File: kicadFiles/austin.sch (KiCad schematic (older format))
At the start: 474 parts, among them J1 TYPE-C-31-M12_13, J5 Conn_01x06_Male, Q1 AO4406AL, SW1 MXSwitch, SW10 MXSwitch, SW100 MXSwitch, SW101 MXSwitch, SW102 MXSwitch, SW103 MXSwitch, SW104 MXSwitch, SW105 MXSwitch, SW106 MXSwitch, SW107 MXSwitch, SW108 MXSwitch, SW109 MXSwitch, SW11 MXSwitch, SW110 MXSwitch, SW111 MXSwitch, SW112 MXSwitch, SW113 MXSwitch, SW114 MXSwitch, SW12 MXSwitch, SW13 MXSwitch, SW14 MXSwitch, SW15 MXSwitch, SW16 MXSwitch, SW17 MXSwitch, SW18 MXSwitch, SW19 MXSwitch, SW2 MXSwitch, SW20 MXSwitch, SW21 MXSwitch, SW22 MXSwitch, SW23 MXSwitch, SW24 MXSwitch, SW25 MXSwitch, SW26 MXSwitch, SW27 MXSwitch, SW28 MXSwitch, SW29 MXSwitch, SW3 MXSwitch, SW30 MXSwitch, SW31 MXSwitch, SW32 MXSwitch, SW33 MXSwitch, SW34 MXSwitch, SW35 MXSwitch, SW36 MXSwitch, SW37 MXSwitch, SW38 MXSwitch, SW39 MXSwitch, SW4 MXSwitch, SW40 MXSwitch, SW41 MXSwitch, SW42 MXSwitch, SW43 MXSwitch, SW44 MXSwitch, SW45 MXSwitch, SW46 MXSwitch, SW47 MXSwitch, SW48 MXSwitch, SW49 MXSwitch, SW5 MXSwitch, SW50 MXSwitch, SW51 MXSwitch, SW52 MXSwitch, SW53 MXSwitch, SW54 MXSwitch, SW55 MXSwitch, SW56 MXSwitch, SW57 MXSwitch, SW59 MXSwitch, SW6 MXSwitch, SW60 MXSwitch, SW61 MXSwitch, SW62 MXSwitch, SW63 MXSwitch, SW64 MXSwitch, SW65 MXSwitch, SW66 MXSwitch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

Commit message: Add LSHIFT ISO key, change LED_PWM pin
- The ISO 1.25U LShift was not added in the pre-Alpha version, even though the ISO Enter was supported. The ISO LShift and slash keys were added to the schematic.

- To accomodate for the change, every key of the fourth row from Z to the up arrow had to be moved a column right.

- The LED_PWM pin had to be reallocated from PB7 to PA6. Although the LEDs are provenly working with the last pin, it does not have hardware PWM, which is desirable. The new pin, PA6, is PWM capable. In order to accomodate this change, the Row3 pin had to be reallocated from PA6 to PB7.
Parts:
- added D34: 1N4148, acheronComponents:D_SOD-123, symbol Device:D
- added SW58: ANSI LShift, acheron_MX:MX225, symbol austin-rescue:MXSwitch-acheronSymbols
- added SW78: ISO Slash, acheron_MX:MX100, symbol austin-rescue:MXSwitch-acheronSymbols
- SW79: value MXSwitch -> ISO LShift; footprint acheron_MX:MX225 -> acheron_MX:MX125
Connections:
- net Col1: now also SW58.1 (Col)
- net Col10: now also SW87.1 (Col); no longer SW88.1 (Col)
- net Col11: now also SW88.1 (Col); no longer SW89.1 (Col)
- net Col12: now also SW89.1 (Col); no longer SW90.1 (Col)
- net Col13: now also SW90.1 (Col); no longer SW91.1 (Col)
- net Col14: now also SW91.1 (Col)
- net Col2: now also SW78.1 (Col); no longer SW80.1 (Col)
- net Col3: now also SW80.1 (Col); no longer SW81.1 (Col)
- net Col4: now also SW81.1 (Col); no longer SW82.1 (Col)
- net Col5: now also SW82.1 (Col); no longer SW83.1 (Col)
- net Col6: now also SW83.1 (Col); no longer SW84.1 (Col)
- net Col7: now also SW84.1 (Col); no longer SW85.1 (Col)
- net Col8: now also SW85.1 (Col); no longer SW86.1 (Col)
- net Col9: now also SW86.1 (Col); no longer SW87.1 (Col)
- net LED_PWM: now also U1.16 (SPI1_MISO/I2S1_MCK/TIM3_CH1/ADCIN6/PA6); no longer U1.43 (I2C1_SDA/PB7)
- net Row3: now also U1.43 (I2C1_SDA/PB7); no longer U1.16 (SPI1_MISO/I2S1_MCK/TIM3_CH1/ADCIN6/PA6)
- net Row5: now also D34.1 (K); no longer D89.1 (K), D91.1 (K)
- net at D79.2 (A), SW79.2 (Row): now also SW58.2 (Row)
- new net: D34.2 (A), SW78.2 (Row)
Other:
- moved on the sheet: D80, D81, D82, D83, D84, D85, D86, D87, D88, D89, D90, D91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

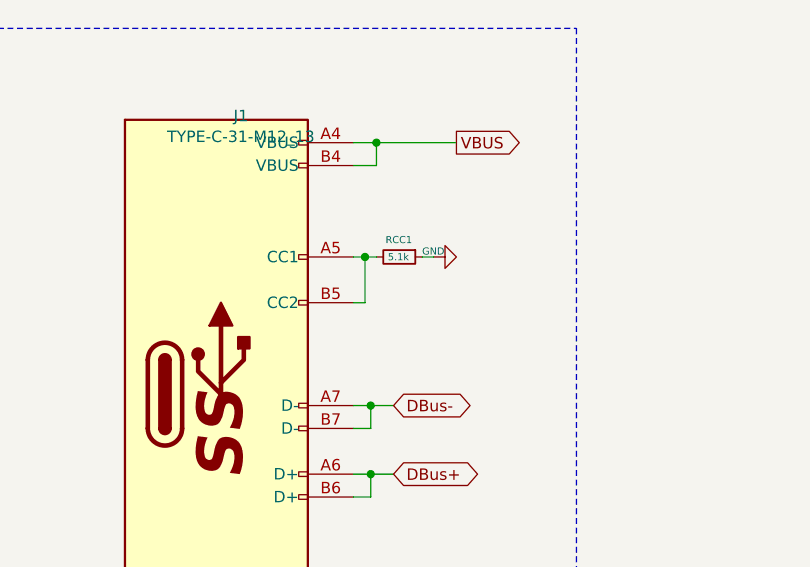
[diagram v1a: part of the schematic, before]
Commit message: Add RCC2
- In version pre-Alpha, the RCC pins were wrongly connected with a single RCC resistor. This is not the right way to implement USBC 3.0 connection; in actuality, each of the two pins should have a single resistor for itself. Hence now there are two RCC resistors.

- The RCC resistors also had their package changed; before they were 1206, and now are 0402. This is meant to save space around the connector area.
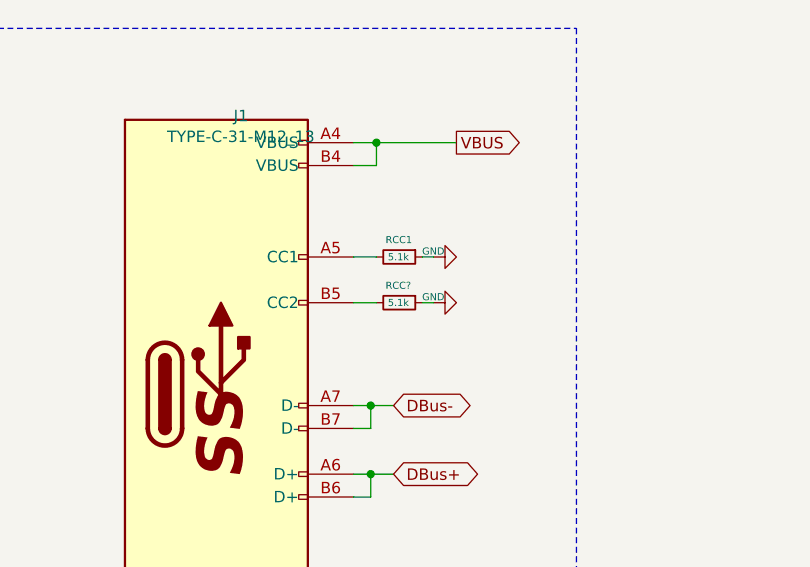
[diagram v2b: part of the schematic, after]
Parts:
- added RCC?: 5.1k, Resistor_SMD:R_0402_1005Metric, symbol Device:R_Small
- RCC1: footprint acheronComponents:R_SMD_1026 -> Resistor_SMD:R_0402_1005Metric
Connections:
- net GND: now also RCC?.1
- net at J1.A5 (CC1), RCC1.2: no longer J1.B5 (CC2)
- new net: J1.B5 (CC2), RCC?.2
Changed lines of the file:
@@
 F 0 "RCC1" V 9350 10115 31  0000 L CNN
 F 1 "5.1k" V 9425 10125 31  0000 L CNN
-F 2 "acheronComponents:R_SMD_1026" H 9425 10175 50  0001 C CNN
+F 2 "Resistor_SMD:R_0402_1005Metric" H 9425 10175 50  0001 C CNN
 F 3 "~" H 9425 10175 50  0001 C CNN
 	1    9425 10175
@@
 	1    0    0    -1
 $EndComp
-Wire Wire Line
-	9225 10175 9275 10175
-Wire Wire Line
-	9275 10175 9275 10375
-Wire Wire Line
-	9275 10375 9225 10375
-Connection ~ 9275 10175
-Wire Wire Line
-	9275 10175 9325 10175
 Text GLabel 11875 12950 2    50   Input ~ 0
 VBUS
@@
 Wire Wire Line
 	3100 6200 3100 7225
+Wire Wire Line
+	9225 10175 9325 10175
+$Comp
+L Device:R_Small RCC?
+U 1 1 5ED7EC85
+P 9425 10375
+F 0 "RCC?" V 9350 10315 31  0000 L CNN
+F 1 "5.1k" V 9425 10325 31  0000 L CNN
+F 2 "Resistor_SMD:R_0402_1005Metric" H 9425 10375 50  0001 C CNN
+F 3 "~" H 9425 10375 50  0001 C CNN
+	1    9425 10375
+	0    1    1    0
+$EndComp
+Wire Wire Line
+	9225 10375 9325 10375
+Wire Wire Line
+	9525 10375 9575 10375
+$Comp
+L power:GND #PWR?
+U 1 1 5EE88A46
+P 9575 10375
+F 0 "#PWR?" H 9575 10125 50  0001 C CNN
+F 1 "GND" V 9600 10425 31  0000 R CNN
+F 2 "" H 9575 10375 50  0001 C CNN
+F 3 "" H 9575 10375 50  0001 C CNN
+	1    9575 10375
+	0    -1   -1   0
+$EndComp
 $EndSCHEMATC

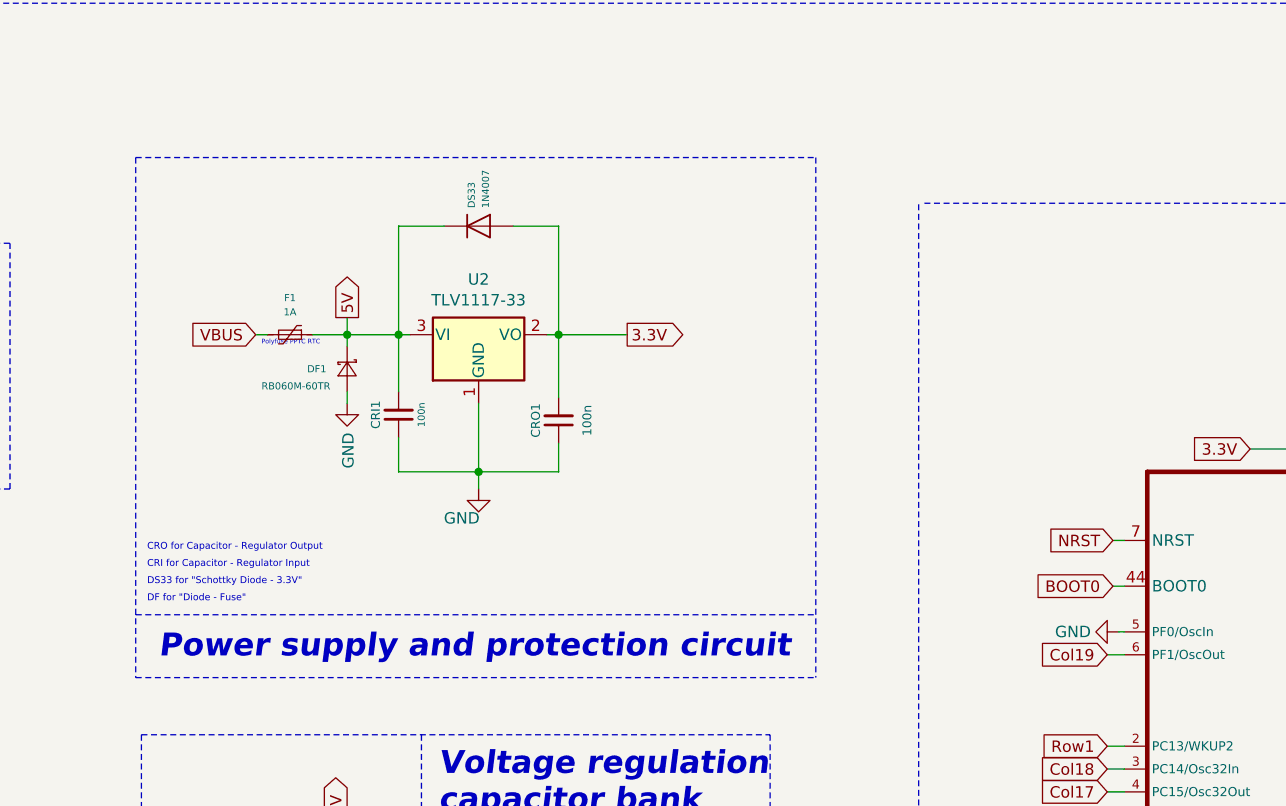
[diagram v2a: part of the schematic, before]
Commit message: Add RF1; change CSI1 to CF1 and to 10uF
- The CSI1 capacitor was changed to 10uF, a more stable value that should offer more voltage regulator for the LDO;

- CSI1 was re-named CF1 for Capacitor-Fuse;

- In order not to leave CF1 charged when the PCB is not powered on, a resistor RF1 was added to discharge CF1  after turn off.
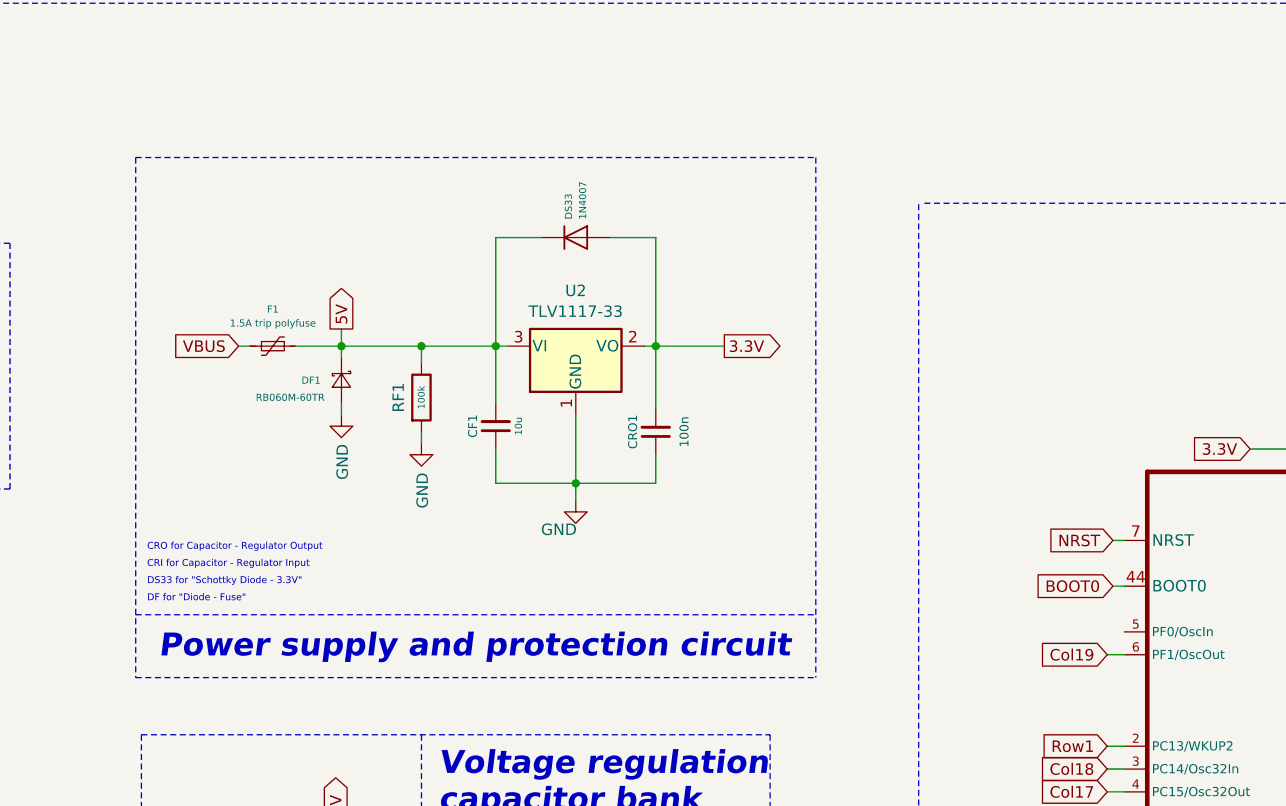
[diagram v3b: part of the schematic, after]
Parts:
- added RF1: 100k, acheronComponents:R_SMD_1026, symbol Device:R
- CF1: renamed from CRI1; value 100n -> 10u
- F1: value 1A -> 1.5A trip polyfuse
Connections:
- net 5V: now also RF1.1
- net GND: now also RF1.2; no longer U1.5 (PF0/OscIn)
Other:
- note removed: "Polyfuse PPTC RTC"
- moved on the sheet: CF1, CRO1, DF1, DS33, F1, U2
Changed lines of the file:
@@
 L Device:Polyfuse_Small F1
 U 1 1 5C25B88F
-P 15775 9525
-F 0 "F1" V 15614 9525 31  0000 C CNN
-F 1 "1A" V 15676 9525 31  0000 C CNN
-F 2 "Fuse:Fuse_1812_4532Metric_Pad1.30x3.40mm_HandSolder" H 15825 9325 50  0001 L CNN
-F 3 "~" H 15775 9525 50  0001 C CNN
-	1    15775 9525
+P 15700 9575
+F 0 "F1" V 15539 9575 31  0000 C CNN
+F 1 "1.5A trip polyfuse" V 15600 9575 31  0000 C CNN
+F 2 "Fuse:Fuse_1812_4532Metric_Pad1.30x3.40mm_HandSolder" H 15750 9375 50  0001 L CNN
+F 3 "~" H 15700 9575 50  0001 C CNN
+	1    15700 9575
 	0    1    1    0
 $EndComp
-Text Notes 15650 9575 0    20   ~ 0
-Polyfuse PPTC RTC
 $Comp
 L Device:D_Schottky_Small DF1
 U 1 1 5C2FFE6A
-P 16025 9675
-F 0 "DF1" V 16025 9500 31  0000 L CNN
-F 1 "RB060M-60TR" V 16100 9300 31  0000 L CNN
-F 2 "acheronComponents:D_SOD-123" V 16025 9675 50  0001 C CNN
-F 3 "~" V 16025 9675 50  0001 C CNN
-	1    16025 9675
+P 16000 9725
+F 0 "DF1" V 16000 9550 31  0000 L CNN
+F 1 "RB060M-60TR" V 16075 9350 31  0000 L CNN
+F 2 "acheronComponents:D_SOD-123" V 16000 9725 50  0001 C CNN
+F 3 "~" V 16000 9725 50  0001 C CNN
+	1    16000 9725
 	0    1    1    0
 $EndComp
 Wire Wire Line
-	15875 9525 16025 9525
+	16000 9575 16000 9625
+Connection ~ 16000 9575
 Wire Wire Line
-	16025 9525 16025 9575
-Connection ~ 16025 9525
-Wire Wire Line
-	16025 9775 16025 9825
+	16000 9825 16000 9875
 $Comp
 L power:GND #PWR016
 U 1 1 5C363806
-P 16025 9825
-F 0 "#PWR016" H 16025 9575 50  0001 C CNN
-F 1 "GND" V 16030 9697 50  0000 R CNN
-F 2 "" H 16025 9825 50  0001 C CNN
-F 3 "" H 16025 9825 50  0001 C CNN
-	1    16025 9825
+P 16000 9875
+F 0 "#PWR016" H 16000 9625 50  0001 C CNN
+F 1 "GND" V 16005 9747 50  0000 R CNN
+F 2 "" H 16000 9875 50  0001 C CNN
+F 3 "" H 16000 9875 50  0001 C CNN
+	1    16000 9875
 	1    0    0    -1
 $EndComp
@@
 $EndComp
 $Comp
-L Device:C_Small CRI1
+L Device:C_Small CF1
 U 1 1 5C44CEDC
-P 16250 9875
-F 0 "CRI1" V 16350 9875 39  0000 C CNN
-F 1 "100n" V 16150 9875 31  0000 C CNN
-F 2 "Capacitor_SMD:C_0805_2012Metric_Pad1.15x1.40mm_HandSolder" H 16250 9875 50  0001 C CNN
-F 3 "~" H 16250 9875 50  0001 C CNN
-	1    16250 9875
+P 16675 9925
+F 0 "CF1" V 16775 9925 39  0000 C CNN
+F 1 "10u" V 16575 9925 31  0000 C CNN
+F 2 "Capacitor_SMD:C_0805_2012Metric_Pad1.15x1.40mm_HandSolder" H 16675 9925 50  0001 C CNN
+F 3 "~" H 16675 9925 50  0001 C CNN
+	1    16675 9925
 	-1   0    0    1
 $EndComp
@@
 L Device:D DS33
 U 1 1 5C44EA7A
-P 16600 9050
-F 0 "DS33" V 16569 9129 31  0000 L CNN
-F 1 "1N4007" V 16631 9129 31  0000 L CNN
-F 2 "acheronComponents:D_SOD-123" H 16600 9050 50  0001 C CNN
-F 3 "~" H 16600 9050 50  0001 C CNN
-	1    16600 9050
+P 17025 9100
+F 0 "DS33" V 16994 9179 31  0000 L CNN
+F 1 "1N4007" V 17056 9179 31  0000 L CNN
+F 2 "acheronComponents:D_SOD-123" H 17025 9100 50  0001 C CNN
+F 3 "~" H 17025 9100 50  0001 C CNN
+	1    17025 9100
 	1    0    0    -1
 $EndComp
@@
 L Device:C_Small CRO1
 U 1 1 5C44DAFA
-P 16950 9900
-F 0 "CRO1" V 17050 9900 39  0000 C CNN
-F 1 "100n" V 16825 9900 39  0000 C CNN
-F 2 "Capacitor_SMD:C_0805_2012Metric_Pad1.15x1.40mm_HandSolder" H 16950 9900 50  0001 C CNN
-F 3 "~" H 16950 9900 50  0001 C CNN
-	1    16950 9900
+P 17375 9950
+F 0 "CRO1" V 17475 9950 39  0000 C CNN
+F 1 "100n" V 17250 9950 39  0000 C CNN
+F 2 "Capacitor_SMD:C_0805_2012Metric_Pad1.15x1.40mm_HandSolder" H 17375 9950 50  0001 C CNN
+F 3 "~" H 17375 9950 50  0001 C CNN
+	1    17375 9950
 	-1   0    0    1
 $EndComp
 Wire Wire Line
-	16950 9525 16950 9800
-Wire Wire Line
-	16300 9525 16250 9525
-Wire Wire Line
-	16250 9525 16250 9775
-Connection ~ 16250 9525
+	17375 9575 17375 9850
 Wire Wire Line
-	16250 9525 16250 9050
+	16675 9575 16675 9825
+Connection ~ 16675 9575
 Wire Wire Line
-	16025 9525 16250 9525
+	16675 9575 16675 9100
 NoConn ~ 9225 11975
 NoConn ~ 9225 11875
@@
 Wire Wire Line
 	9300 10925 9300 10825
-Text GLabel 17250 9525 2    50   Output ~ 0
+Text GLabel 17675 9575 2    50   Output ~ 0
 3.3V
 Text GLabel 19375 12125 0    50   BiDi ~ 0
@@
 	19375 12025 19425 12025
 Wire Wire Line
-	16250 9975 16250 10125
+	16675 10025 16675 10175
 Wire Wire Line
-	16950 10125 16950 10000
+	17375 10175 17375 10050
 Wire Wire Line
-	16600 9825 16600 10125
-Connection ~ 16600 10125
+	17025 9875 17025 10175
+Connection ~ 17025 10175
 Wire Wire Line
-	16900 9525 16950 9525
+	17325 9575 17375 9575
 $Comp
 L power:GND #PWR018
 U 1 1 5D9C16B4
-P 16600 10200
-F 0 "#PWR018" H 16600 9950 50  0001 C CNN
-F 1 "GND" H 16605 10072 50  0000 R CNN
-F 2 "" H 16600 10200 50  0001 C CNN
-F 3 "" H 16600 10200 50  0001 C CNN
-	1    16600 10200
+P 17025 10250
+F 0 "#PWR018" H 17025 10000 50  0001 C CNN
+F 1 "GND" H 17030 10122 50  0000 R CNN
+F 2 "" H 17025 10250 50  0001 C CNN
+F 3 "" H 17025 10250 50  0001 C CNN
+	1    17025 10250
 	1    0    0    -1
 $EndComp
 Wire Wire Line
-	16600 10200 16600 10125
+	17025 10250 17025 10175
 Text GLabel 19975 10025 0    50   Input ~ 0
 3.3V
@@
 Text GLabel 9675 9675 2    50   Output ~ 0
 VBUS
-Text GLabel 15625 9525 0    50   Input ~ 0
+Text GLabel 15550 9575 0    50   Input ~ 0
 VBUS
 Wire Wire Line
-	15625 9525 15675 9525
+	15550 9575 15600 9575
 Text Notes 15200 10950 0    100  Italic 20
 Power supply and protection circuit
 Wire Wire Line
 	9225 9675 9325 9675
-Text GLabel 16025 9450 1    50   Output ~ 0
+Text GLabel 16000 9500 1    50   Output ~ 0
 5V
 Wire Wire Line
-	16025 9450 16025 9525
+	16000 9500 16000 9575
 Text GLabel 775  8900 1    50   Input ~ 0
 5V
@@
 Voltage regulation\ncapacitor bank\n
 Wire Wire Line
-	16750 9050 16950 9050
+	17175 9100 17375 9100
 Wire Wire Line
-	16250 9050 16450 9050
+	16675 9100 16875 9100
 Wire Wire Line
-	16950 9525 16950 9050
-Connection ~ 16950 9525
+	17375 9575 17375 9100
+Connection ~ 17375 9575
 Wire Wire Line
-	16600 10125 16950 10125
+	17025 10175 17375 10175
 Wire Wire Line
-	16950 9525 17250 9525
+	17375 9575 17675 9575
 Wire Wire Line
-	16600 10125 16250 10125
+	17025 10175 16675 10175
 Text Notes 8000 13175 0    50   ~ 0
 Shield\nnet
@@
 L Regulator_Linear:TLV1117-33 U2
 U 1 1 5D21E92D
-P 16600 9525
-F 0 "U2" H 16600 9767 50  0000 C CNN
-F 1 "TLV1117-33" H 16600 9676 50  0000 C CNN
-F 2 "Package_TO_SOT_SMD:SOT-223-3_TabPin2" H 16600 9525 50  0001 C CNN
-F 3 "http://www.ti.com/lit/ds/symlink/tlv1117.pdf" H 16600 9525 50  0001 C CNN
-	1    16600 9525
+P 17025 9575
+F 0 "U2" H 17025 9817 50  0000 C CNN
+F 1 "TLV1117-33" H 17025 9726 50  0000 C CNN
+F 2 "Package_TO_SOT_SMD:SOT-223-3_TabPin2" H 17025 9575 50  0001 C CNN
+F 3 "http://www.ti.com/lit/ds/symlink/tlv1117.pdf" H 17025 9575 50  0001 C CNN
+	1    17025 9575
 	1    0    0    -1
 $EndComp
@@
 	1    0    0    -1
 $EndComp
-$Comp
-L power:GND #PWR0109
-U 1 1 5DCDF6A1
-P 19400 10825
-F 0 "#PWR0109" H 19400 10575 50  0001 C CNN
-F 1 "GND" V 19400 10625 50  0000 C CNN
-F 2 "" H 19400 10825 50  0001 C CNN
-F 3 "" H 19400 10825 50  0001 C CNN
-	1    19400 10825
-	0    1    1    0
-$EndComp
-Wire Wire Line
-	19400 10825 19425 10825
 Wire Notes Line
 	7975 12250 8450 12250
@@
 	0    -1   -1   0
 $EndComp
+$Comp
+L Device:R RF1
+U 1 1 5F1A5DBD
+P 16350 9800
+F 0 "RF1" V 16250 9800 50  0000 C CNN
+F 1 "100k" V 16350 9800 30  0000 C CNN
+F 2 "acheronComponents:R_SMD_1026" V 16280 9800 50  0001 C CNN
+F 3 "~" H 16350 9800 50  0001 C CNN
+	1    16350 9800
+	1    0    0    -1
+$EndComp
+Wire Wire Line
+	16350 9575 16350 9650
+Wire Wire Line
+	16000 9575 16350 9575
+Wire Wire Line
+	16350 9950 16350 10000
+$Comp
+L power:GND #PWR?
+U 1 1 5F2B0631
+P 16350 10000
+F 0 "#PWR?" H 16350 9750 50  0001 C CNN
+F 1 "GND" V 16355 9872 50  0000 R CNN
+F 2 "" H 16350 10000 50  0001 C CNN
+F 3 "" H 16350 10000 50  0001 C CNN
+	1    16350 10000
+	1    0    0    -1
+$EndComp
+Wire Wire Line
+	16350 9575 16675 9575
+Connection ~ 16350 9575
+Wire Wire Line
+	15800 9575 16000 9575
+Wire Wire Line
+	16675 9575 16725 9575
 $EndSCHEMATC
